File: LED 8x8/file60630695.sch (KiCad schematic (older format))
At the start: 4 parts, among them U601 74HC164, U602 74HC164

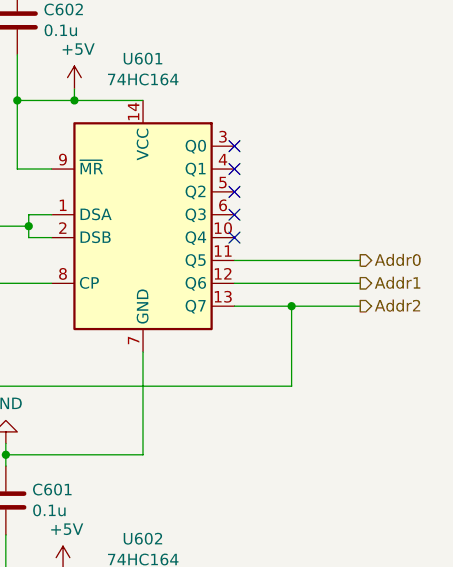
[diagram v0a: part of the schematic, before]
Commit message: Had address register connected backwards on LED 8x8
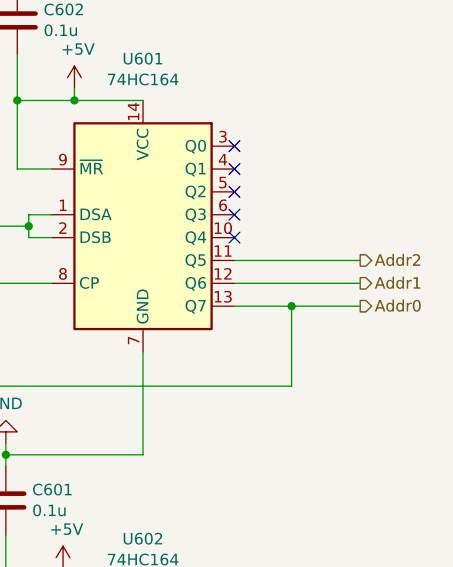
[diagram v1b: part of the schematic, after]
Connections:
- net Addr0: now also U601.13 (Q7), U602.1 (DSA), U602.2 (DSB); no longer U601.11 (Q5)
- net Addr2: now also U601.11 (Q5); no longer U601.13 (Q7), U602.1 (DSA), U602.2 (DSB)
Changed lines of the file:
@@
 Connection ~ 2100 2000
 Text HLabel 3600 2700 2    50   Output ~ 0
-Addr0
+Addr2
 Text HLabel 3600 2800 2    50   Output ~ 0
 Addr1
 Text HLabel 3600 2900 2    50   Output ~ 0
-Addr2
+Addr0
 Wire Wire Line
 	3050 2700 3600 2700
